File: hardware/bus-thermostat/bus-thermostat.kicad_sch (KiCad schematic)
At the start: 2 parts, among them J1 Screw_Terminal_01x05, J2 Screw_Terminal_01x02

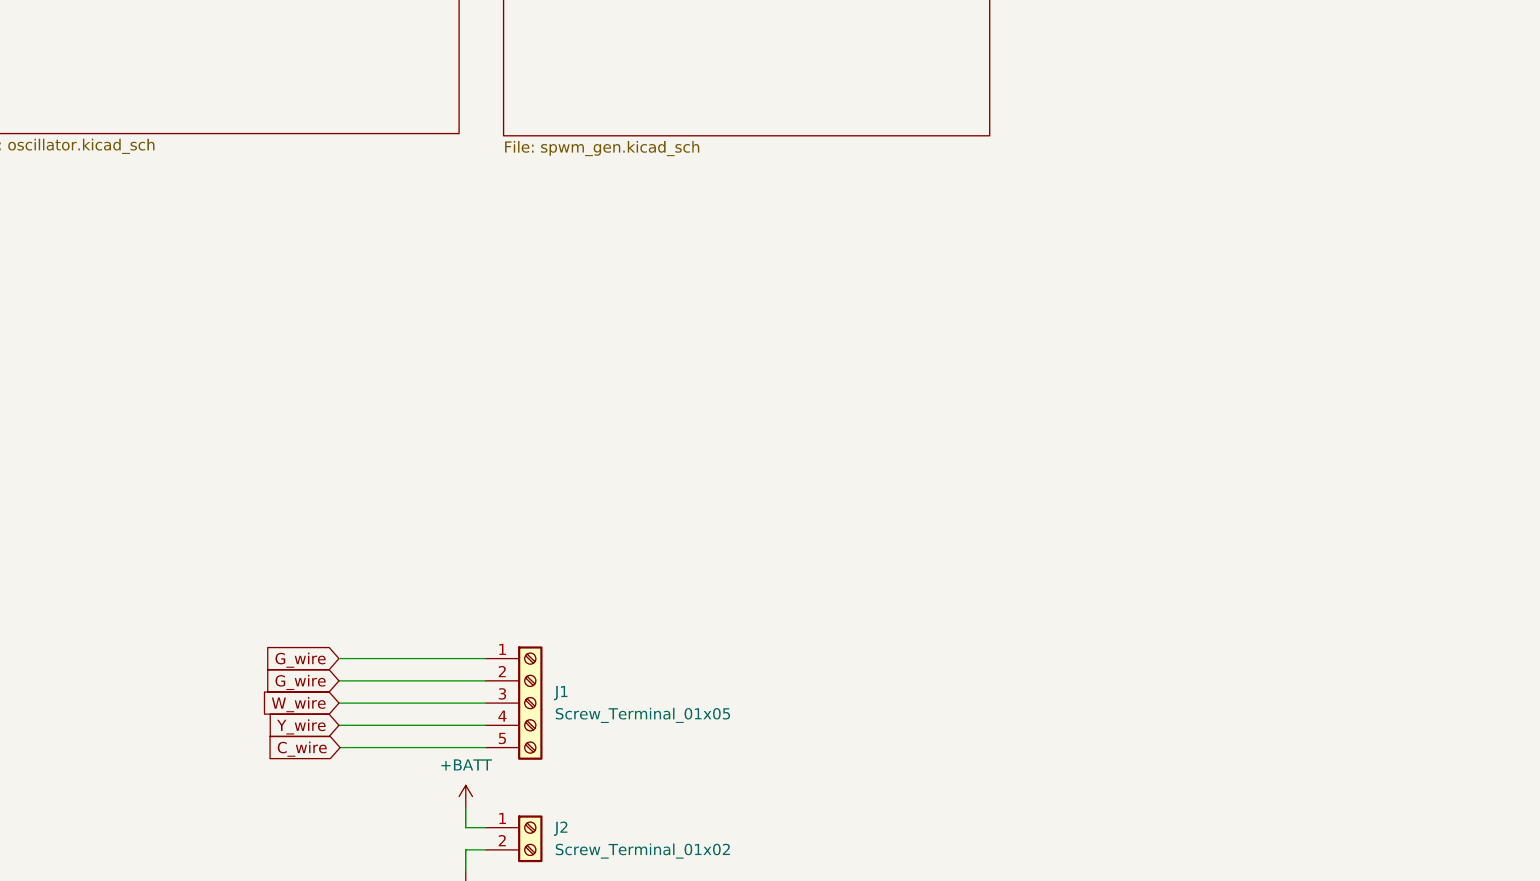
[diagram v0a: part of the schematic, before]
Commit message: Fix oscillator, add fan controller/thermostat and its IOs.
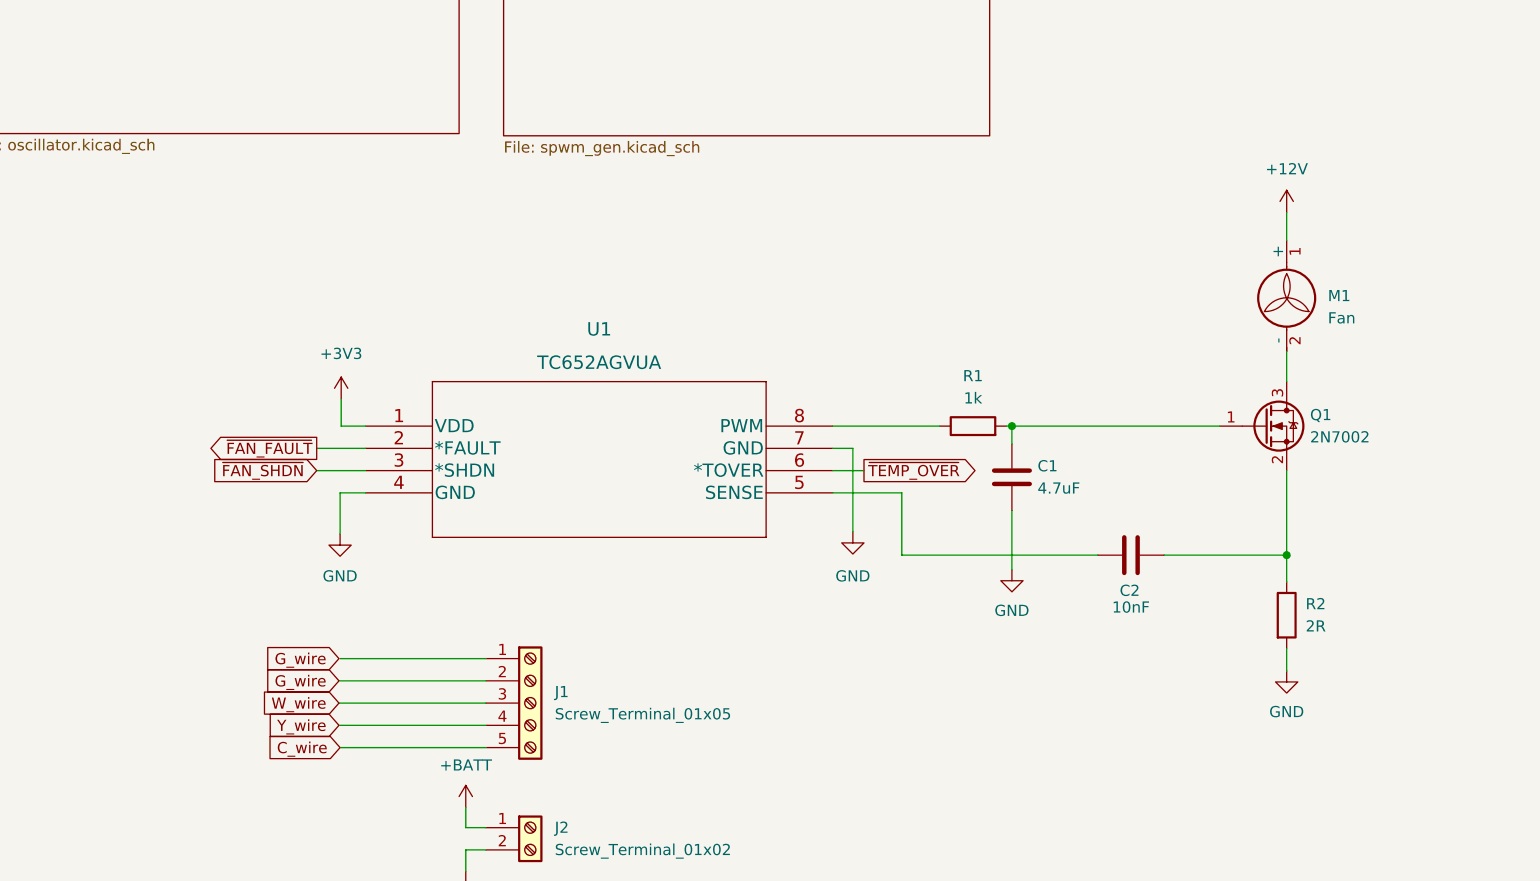
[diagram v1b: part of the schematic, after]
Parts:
- added C1: 4.7uF, Capacitor_SMD:C_0805_2012Metric_Pad1.18x1.45mm_HandSolder, symbol Device:C
- added C2: 10nF, Capacitor_SMD:C_0805_2012Metric_Pad1.18x1.45mm_HandSolder, symbol Device:C
- added M1: Fan, Connector_PinHeader_1.00mm:PinHeader_1x02_P1.00mm_Vertical, symbol Motor:Fan
- added Q1: 2N7002, Package_TO_SOT_SMD:SOT-23, symbol Transistor_FET:2N7002
- added R1: 1k, Resistor_SMD:R_0805_2012Metric_Pad1.20x1.40mm_HandSolder, symbol Device:R
- added R2: 2R, Resistor_SMD:R_0805_2012Metric_Pad1.20x1.40mm_HandSolder, symbol Device:R
- added U1: TC652AGVUA, UltraLibrarian:TC652AGVUA, symbol UltraLibrarian:TC652AGVUA
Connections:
- net GND: now also C1.2, R2.2, U1.4 (GND), U1.7 (GND)
- new net: C1.1, Q1.1 (G), R1.2
- new net: C2.2, Q1.2 (S), R2.1
- new net: M1.2 (-), Q1.3 (D)
- new net: C2.1, U1.5 (SENSE)
- new net: R1.1, U1.8 (PWM)
- new net +12V: M1.1 (+)
- new net +3V3: U1.1 (VDD)
- new net ~{FAN_FAULT}: U1.2 (*FAULT)
- new net ~{FAN_SHDN}: U1.3 (*SHDN)
- new net ~{TEMP_OVER}: U1.6 (*TOVER)
